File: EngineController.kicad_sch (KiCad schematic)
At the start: 35 parts, among them J1 RBUS, U1 ESP32-S3, Y1 R940000171

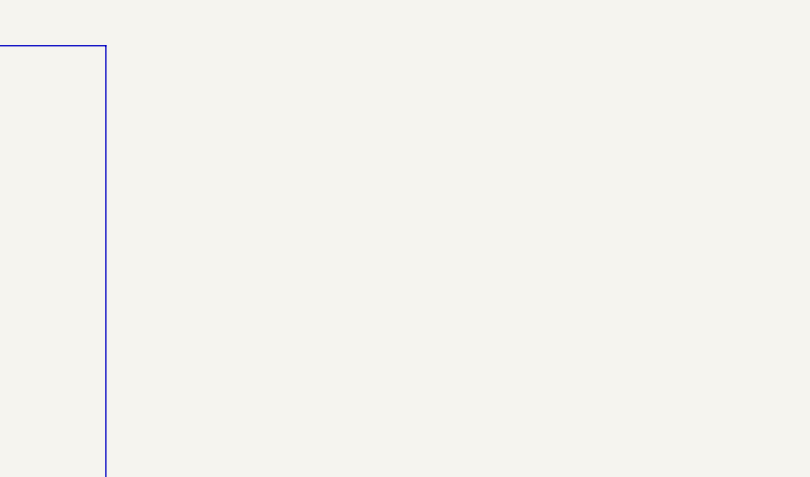
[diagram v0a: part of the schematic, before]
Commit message: Engine Controller Board: Added in Buck
Added in buck for chad and modified resistors to have output of 7.4V and 6V instead of 8.4V
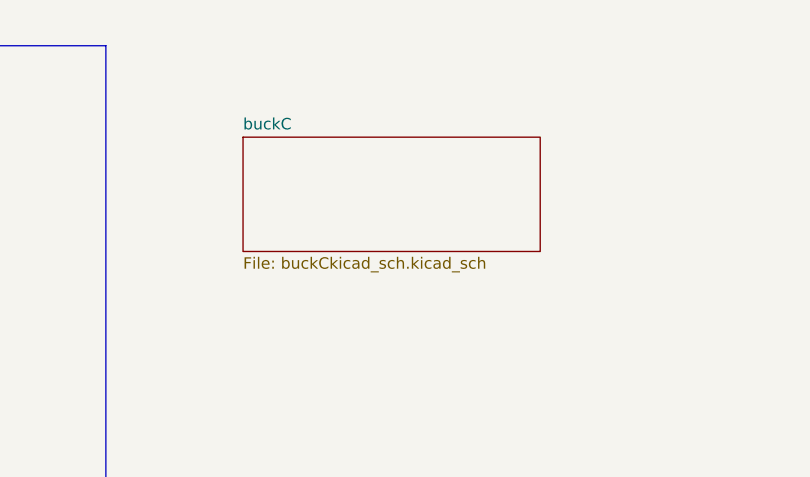
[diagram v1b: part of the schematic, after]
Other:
- added sheet buckC (buckCkicad_sch.kicad_sch)

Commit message: Xavier: Updated Engine Controller
Added in the actuators
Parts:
- added R25: 2.2k, Resistor_SMD:R_0402_1005Metric, symbol Device:R_Small
- added R5: 1.5k, Resistor_SMD:R_0402_1005Metric, symbol Device:R_Small
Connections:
- net GND: now also R25.1
- net BuckPGOOD: now reaches U1.37 (SPICLK_P/GPIO47)
- net BuckPGOOD: now also R25.2, R5.1
- net Servo1PWM: now reaches U1.41 (GPIO36)
- net Servo2PWM: now reaches U1.42 (GPIO37)
- net BUCK_EN: now reaches U1.43 (GPIO38)
- new net buckC/PGOOD: R5.2
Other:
- added sheet actuators (actuators.kicad_sch)
- sheet buckC ports: added BUCK_EN, PGOOD; removed none
- note added: "ServoV_LOG"
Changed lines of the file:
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@@
+    (stroke (width 0) (type default))
+  )
+  (wire (pts (xy 213.36 58.42) (xy 219.71 58.42))
     (stroke (width 0) (type default))
   )
@@
     (stroke (width 0) (type default))
   )
+  (wire (pts (xy 213.36 54.61) (xy 219.71 54.61))
+    (stroke (width 0) (type default))
+  )
   (wire (pts (xy 16.51 170.18) (xy 16.51 171.45))
     (stroke (width 0) (type default))
@@
     (stroke (width 0) (type default))
   )
+  (wire (pts (xy 213.36 62.23) (xy 219.71 62.23))
+    (stroke (width 0) (type default))
+  )
   (wire (pts (xy 44.45 135.89) (xy 46.99 135.89))
     (stroke (width 0) (type default))
@@
     (stroke (width 0) (type default))
   )
+  (wire (pts (xy 218.44 30.48) (xy 218.44 34.29))
+    (stroke (width 0) (type default))
+  )
   (wire (pts (xy 278.13 33.02) (xy 273.05 33.02))
     (stroke (width 0) (type default))
@@
     (stroke (width 0) (type default))
   )
+  (wire (pts (xy 215.9 21.59) (xy 226.06 21.59))
+    (stroke (width 0) (type default))
+  )
   (wire (pts (xy 107.95 187.96) (xy 115.57 187.96))
     (stroke (width 0) (type default))
@@
   )
   (wire (pts (xy 34.29 140.97) (xy 46.99 140.97))
+    (stroke (width 0) (type default))
+  )
+  (wire (pts (xy 215.9 25.4) (xy 218.44 25.4))
     (stroke (width 0) (type default))
   )
@@
     (effects (font (size 1.27 1.27)) (justify left bottom))
   )
+  (text "ServoV_LOG" (at 219.71 62.23 0)
+    (effects (font (size 1.27 1.27)) (justify left bottom))
+  )
   (text "CAN + is CAN High\nCAN - is CAN LOW\nNamed with a + and - as it\nis a KiCad requirement to\nroute differential tracks\n"
     (at 123.19 195.58 0)
@@
     (effects (font (size 1.27 1.27)) (justify right bottom))
   )
+  (text "ServoV_LOG" (at 135.89 100.33 0)
+    (effects (font (size 1.27 1.27)) (justify left bottom))
+  )
+  (label "Servo1PWM" (at 135.89 102.87 0) (fields_autoplaced)
+    (effects (font (size 1.27 1.27)) (justify left bottom))
+  )
   (label "CHIP_PU" (at 36.83 165.1 180) (fields_autoplaced)
     (effects (font (size 1.27 1.27)) (justify right bottom))
   )
+  (label "Servo1PWM" (at 219.71 58.42 0) (fields_autoplaced)
+    (effects (font (size 1.27 1.27)) (justify left bottom))
+  )
   (label "CAN+" (at 115.57 185.42 0) (fields_autoplaced)
     (effects (font (size 1.27 1.27)) (justify left bottom))
@@
     (effects (font (size 1.27 1.27)) (justify left bottom))
   )
+  (label "BuckPGOOD" (at 135.89 118.11 0) (fields_autoplaced)
+    (effects (font (size 1.27 1.27)) (justify left bottom))
+  )
   (label "RXD" (at 29.21 43.18 0) (fields_autoplaced)
+    (effects (font (size 1.27 1.27)) (justify left bottom))
+  )
+  (label "Servo2PWM" (at 219.71 54.61 0) (fields_autoplaced)
     (effects (font (size 1.27 1.27)) (justify left bottom))
   )
@@
     (effects (font (size 1.27 1.27)) (justify right bottom))
   )
+  (label "BUCK_EN" (at 226.06 21.59 180) (fields_autoplaced)
+    (effects (font (size 1.27 1.27)) (justify right bottom))
+  )
+  (label "BUCK_EN" (at 135.89 107.95 0) (fields_autoplaced)
+    (effects (font (size 1.27 1.27)) (justify left bottom))
+  )
   (label "RXD" (at 64.77 115.57 180) (fields_autoplaced)
     (effects (font (size 1.27 1.27)) (justify right bottom))
@@
     (effects (font (size 1.27 1.27)) (justify left bottom))
   )
+  (label "Servo2PWM" (at 135.89 105.41 0) (fields_autoplaced)
+    (effects (font (size 1.27 1.27)) (justify left bottom))
+  )
   (label "CAN_RX" (at 115.57 182.88 0) (fields_autoplaced)
     (effects (font (size 1.27 1.27)) (justify left bottom))
@@
   )
   (label "CAN-" (at 115.57 187.96 0) (fields_autoplaced)
+    (effects (font (size 1.27 1.27)) (justify left bottom))
+  )
+  (label "BuckPGOOD" (at 218.44 33.02 0) (fields_autoplaced)
     (effects (font (size 1.27 1.27)) (justify left bottom))
   )
@@
     )
   )
+  (symbol (lib_id "power:GND") (at 218.44 39.37 0) (unit 1)
+    (in_bom yes) (on_board yes) (dnp no)
+    (property "Reference" "#PWR028" (at 218.44 45.72 0)
+      (effects (font (size 1.27 1.27)) hide)
+    )
+    (property "Value" "GND" (at 218.567 43.7642 0)
+      (effects (font (size 1.27 1.27)))
+    )
+    (property "Footprint" "" (at 218.44 39.37 0)
+      (effects (font (size 1.27 1.27)) hide)
+    )
+    (property "Datasheet" "" (at 218.44 39.37 0)
+      (effects (font (size 1.27 1.27)) hide)
+    )
+    (pin "1")
+    (instances
+      (project "EngineController"
+        (path "/7db990e4-92e1-4f99-b4d2-435bbec1ba83"
+          (reference "#PWR028") (unit 1)
+        )
+      )
+    )
+  )
   (symbol (lib_id "power:GND") (at 167.64 132.08 0) (unit 1)
     (in_bom yes) (on_board yes) (dnp no)
@@
         (path "/7db990e4-92e1-4f99-b4d2-435bbec1ba83"
           (reference "#PWR011") (unit 1)
+        )
+      )
+    )
+  )
+  (symbol (lib_id "Device:R_Small") (at 218.44 27.94 180) (unit 1)
+    (in_bom yes) (on_board yes) (dnp no)
+    (property "Reference" "R5" (at 223.4184 27.94 90)
+      (effects (font (size 1.27 1.27)))
+    )
+    (property "Value" "1.5k" (at 221.107 27.94 90)
+      (effects (font (size 1.27 1.27)))
+    )
+    (property "Footprint" "Resistor_SMD:R_0402_1005Metric" (at 218.44 27.94 0)
+      (effects (font (size 1.27 1.27)) hide)
+    )
+    (property "Datasheet" "~" (at 218.44 27.94 0)
+      (effects (font (size 1.27 1.27)) hide)
+    )
+    (pin "1")
+    (pin "2")
+    (instances
+      (project "EngineController"
+        (path "/7db990e4-92e1-4f99-b4d2-435bbec1ba83"
+          (reference "R5") (unit 1)
         )
       )
@@
     )
   )
+  (symbol (lib_id "Device:R_Small") (at 218.44 36.83 180) (unit 1)
+    (in_bom yes) (on_board yes) (dnp no)
+    (property "Reference" "R25" (at 223.4184 36.83 90)
+      (effects (font (size 1.27 1.27)))
+    )
+    (property "Value" "2.2k" (at 221.107 36.83 90)
+      (effects (font (size 1.27 1.27)))
+    )
+    (property "Footprint" "Resistor_SMD:R_0402_1005Metric" (at 218.44 36.83 0)
+      (effects (font (size 1.27 1.27)) hide)
+    )
+    (property "Datasheet" "~" (at 218.44 36.83 0)
+      (effects (font (size 1.27 1.27)) hide)
+    )
+    (pin "1")
+    (pin "2")
+    (instances
+      (project "EngineController"
+        (path "/7db990e4-92e1-4f99-b4d2-435bbec1ba83"
+          (reference "R25") (unit 1)
+        )
+      )
+    )
+  )
   (symbol (lib_id "power:GND") (at 270.51 33.02 0) (unit 1)
     (in_bom yes) (on_board yes) (dnp no)
@@
     )
   )
-  (sheet (at 190.5 22.86) (size 33.02 12.7) (fields_autoplaced)
+  (sheet (at 182.88 49.53) (size 30.48 15.24) (fields_autoplaced)
     (stroke (width 0.1524) (type solid))
     (fill (color 0 0 0 0.0000))
-    (property "Sheetname" "buckC" (at 190.5 22.1484 0)
+    (property "Sheetname" "actuators" (at 182.88 48.8184 0)
       (effects (font (size 1.27 1.27)) (justify left bottom))
     )
-    (property "Sheetfile" "buckCkicad_sch.kicad_sch" (at 190.5 36.1446 0)
+    (property "Sheetfile" "actuators.kicad_sch" (at 182.88 65.3546 0)
       (effects (font (size 1.27 1.27)) (justify left top))
     )
-    (instances
+    (pin "SERVO2" bidirectional (at 213.36 54.61 0)
+      (effects (font (size 1.27 1.27)) (justify right))
+    )
+    (pin "SERVO1" bidirectional (at 213.36 58.42 0)
+      (effects (font (size 1.27 1.27)) (justify right))
+    )
+    (pin "SERVO_LOG" output (at 213.36 62.23 0)
+      (effects (font (size 1.27 1.27)) (justify right))
+    )
+    (instances
+      (project "EngineController"
+        (path "/7db990e4-92e1-4f99-b4d2-435bbec1ba83" (page "6"))
+      )
+    )
+  )
+  (sheet (at 182.88 17.78) (size 33.02 12.7) (fields_autoplaced)
+    (stroke (width 0.1524) (type solid))
+    (fill (color 0 0 0 0.0000))
+    (property "Sheetname" "buckC" (at 182.88 17.0684 0)
+      (effects (font (size 1.27 1.27)) (justify left bottom))
+    )
+    (property "Sheetfile" "buckCkicad_sch.kicad_sch" (at 182.88 31.0646 0)
+      (effects (font (size 1.27 1.27)) (justify left top))
+    )
+    (pin "PGOOD" output (at 215.9 25.4 0)
+      (effects (font (size 1.27 1.27)) (justify right))
+    )
+    (pin "BUCK_EN" input (at 215.9 21.59 0)
+      (effects (font (size 1.27 1.27)) (justify right))
+    )
+    (instances

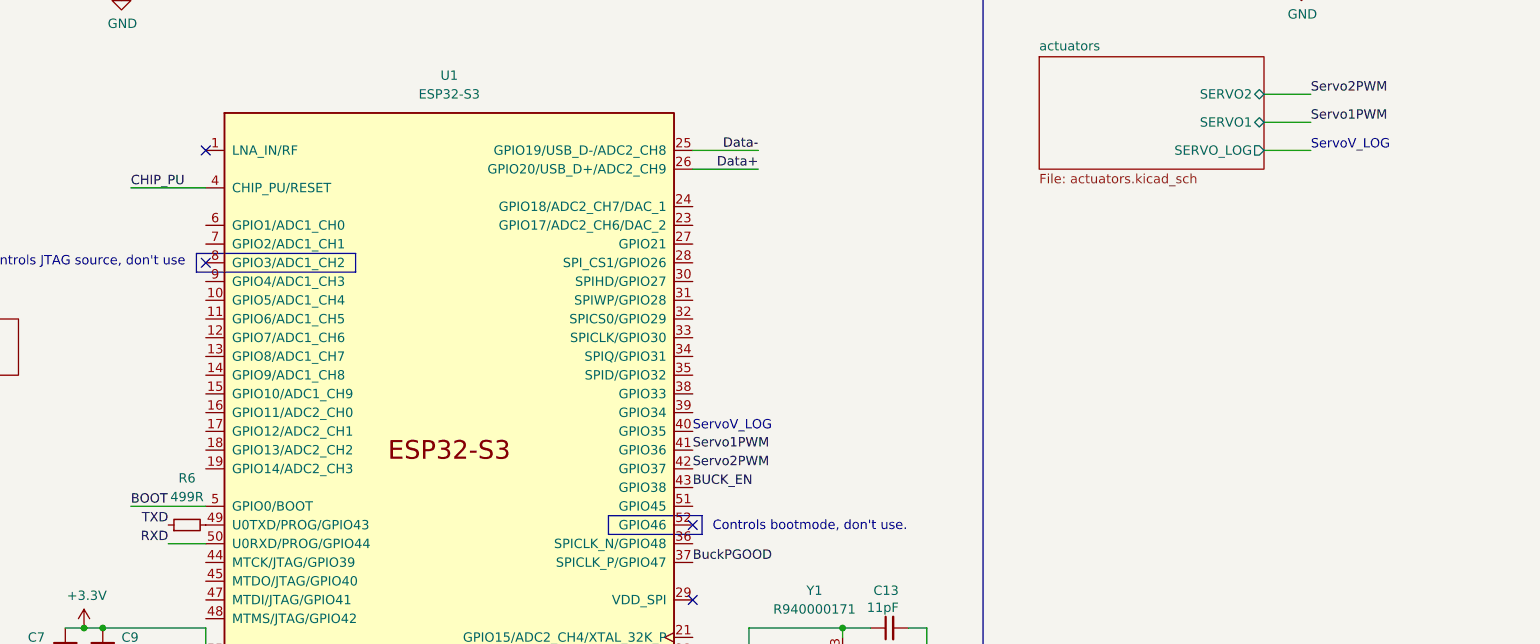
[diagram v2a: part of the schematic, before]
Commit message: Engine Controller: Added in ads and pressure sensor
Circuit for both 5v and 10v
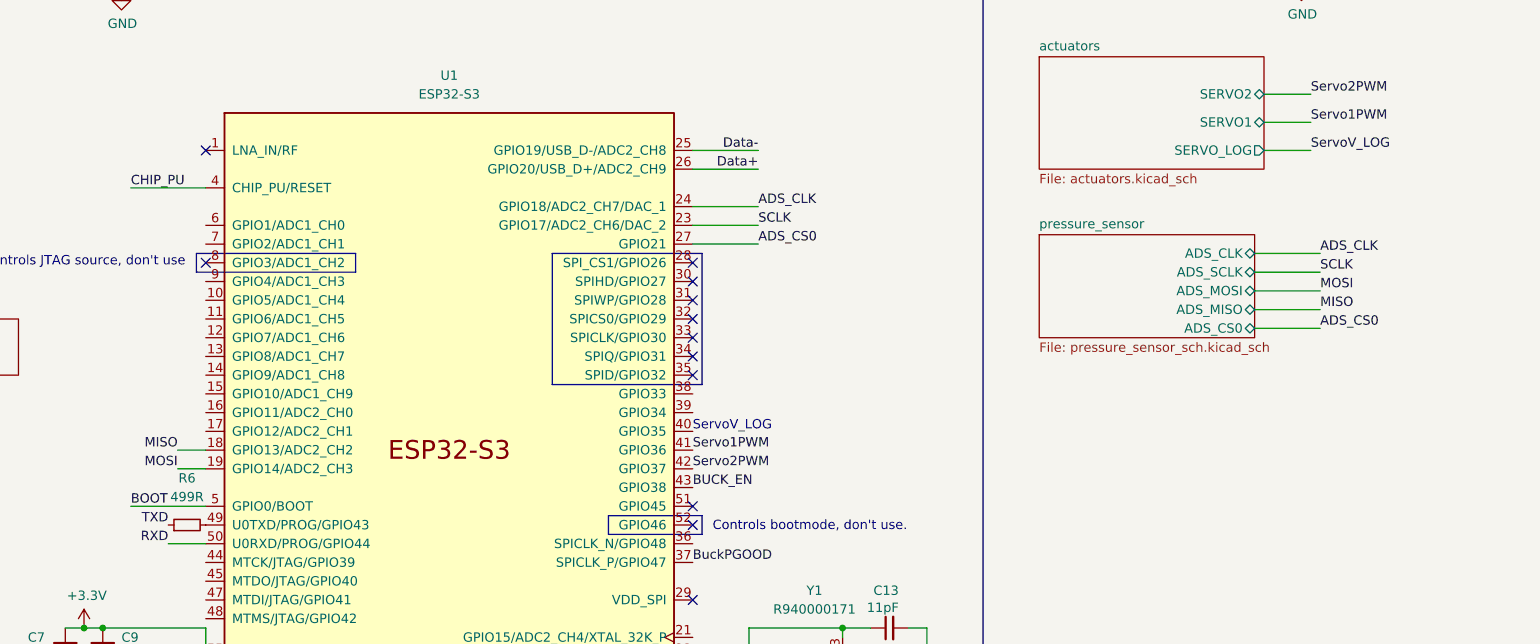
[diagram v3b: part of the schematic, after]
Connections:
- net MISO: now reaches U1.18 (GPIO13/ADC2_CH2)
- net MOSI: now reaches U1.19 (GPIO14/ADC2_CH3)
- net SCLK: now reaches U1.23 (GPIO17/ADC2_CH6/DAC_2)
- net ADS_CLK: now reaches U1.24 (GPIO18/ADC2_CH7/DAC_1)
- net ADS_CS0: now reaches U1.27 (GPIO21)
- no-connect marks 4 -> 12
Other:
- added sheet pressure_sensor (pressure_sensor_sch.kicad_sch)
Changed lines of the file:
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@@
   (junction (at 69.85 135.89) (diameter 0) (color 0 0 0 0)
   )
+  (no_connect (at 135.89 90.17))
+  (no_connect (at 135.89 82.55))
+  (no_connect (at 135.89 80.01))
   (no_connect (at 69.85 77.47))
+  (no_connect (at 135.89 85.09))
   (no_connect (at 69.85 62.23))
   (no_connect (at 135.89 113.03))
+  (no_connect (at 135.89 87.63))
+  (no_connect (at 135.89 92.71))
+  (no_connect (at 135.89 77.47))
   (no_connect (at 135.89 123.19))
+  (no_connect (at 135.89 110.49))
   (wire (pts (xy 30.48 191.77) (xy 30.48 190.5))
     (stroke (width 0) (type default))
@@
     (stroke (width 0) (type default))
   )
+  (wire (pts (xy 212.09 83.82) (xy 220.98 83.82))
+    (stroke (width 0) (type default))
+  )
+  (wire (pts (xy 212.09 81.28) (xy 220.98 81.28))
+    (stroke (width 0) (type default))
+  )
+  (wire (pts (xy 66.04 105.41) (xy 69.85 105.41))
+    (stroke (width 0) (type default))
+  )
   (wire (pts (xy 160.02 127) (xy 156.21 127))
     (stroke (width 0) (type default))
@@
     (stroke (width 0) (type default))
   )
+  (polyline (pts (xy 137.16 76.2) (xy 137.16 93.98))
+    (stroke (width 0) (type default))
+  )
   (wire (pts (xy 29.21 135.89) (xy 34.29 135.89))
     (stroke (width 0) (type default))
@@
     (stroke (width 0) (type default))
   )
+  (wire (pts (xy 135.89 72.39) (xy 144.78 72.39))
+    (stroke (width 0) (type default))
+  )
   (wire (pts (xy 57.15 147.32) (xy 59.69 147.32))
     (stroke (width 0) (type default))
@@
     (stroke (width 0) (type default))
   )
+  (polyline (pts (xy 137.16 93.98) (xy 116.84 93.98))
+    (stroke (width 0) (type default))
+  )
   (wire (pts (xy 156.21 127) (xy 156.21 128.27))
     (stroke (width 0) (type default))
@@
     (stroke (width 0) (type default))
   )
+  (wire (pts (xy 212.09 76.2) (xy 220.98 76.2))
+    (stroke (width 0) (type default))
+  )
   (wire (pts (xy 69.85 130.81) (xy 69.85 133.35))
     (stroke (width 0) (type default))
@@
     (stroke (width 0) (type default))
   )
+  (polyline (pts (xy 116.84 76.2) (xy 116.84 93.98))
+    (stroke (width 0) (type default))
+  )
   (wire (pts (xy 278.13 33.02) (xy 273.05 33.02))
     (stroke (width 0) (type default))
@@
     (stroke (width 0) (type default))
   )
+  (polyline (pts (xy 137.16 76.2) (xy 116.84 76.2))
+    (stroke (width 0) (type default))
+  )
+  (wire (pts (xy 212.09 78.74) (xy 220.98 78.74))
+    (stroke (width 0) (type default))
+  )
   (wire (pts (xy 167.64 127) (xy 167.64 132.08))
     (stroke (width 0) (type default))
@@
     (stroke (width 0) (type default))
   )
+  (wire (pts (xy 135.89 69.85) (xy 144.78 69.85))
+    (stroke (width 0) (type default))
+  )
   (wire (pts (xy 53.34 127) (xy 55.88 127))
     (stroke (width 0) (type default))
@@
     (stroke (width 0) (type default))
   )
+  (wire (pts (xy 66.04 102.87) (xy 69.85 102.87))
+    (stroke (width 0) (type default))
+  )
   (wire (pts (xy 69.85 142.24) (xy 69.85 140.97))
     (stroke (width 0) (type default))
@@
     (stroke (width 0) (type default))
   )
+  (wire (pts (xy 135.89 74.93) (xy 144.78 74.93))
+    (stroke (width 0) (type default))
+  )
   (wire (pts (xy 16.51 165.1) (xy 24.13 165.1))
     (stroke (width 0) (type default))
   )
   (polyline (pts (xy 175.26 198.12) (xy 12.7 198.12))
+    (stroke (width 0) (type default))
+  )
+  (wire (pts (xy 212.09 86.36) (xy 220.98 86.36))
     (stroke (width 0) (type default))
   )
@@
     (effects (font (size 1.27 1.27)) (justify left bottom))
   )
-  (text "ServoV_LOG" (at 219.71 62.23 0)
-    (effects (font (size 1.27 1.27)) (justify left bottom))
-  )
   (text "CAN + is CAN High\nCAN - is CAN LOW\nNamed with a + and - as it\nis a KiCad requirement to\nroute differential tracks\n"
     (at 123.19 195.58 0)
@@
     (effects (font (size 1.27 1.27)) (justify left bottom))
   )
+  (label "MOSI" (at 220.98 81.28 0) (fields_autoplaced)
+    (effects (font (size 1.27 1.27)) (justify left bottom))
+  )
   (label "Servo1PWM" (at 135.89 102.87 0) (fields_autoplaced)
     (effects (font (size 1.27 1.27)) (justify left bottom))
@@
     (effects (font (size 1.27 1.27)) (justify left bottom))
   )
+  (label "MISO" (at 220.98 83.82 0) (fields_autoplaced)
+    (effects (font (size 1.27 1.27)) (justify left bottom))
+  )
+  (label "SCLK" (at 220.98 78.74 0) (fields_autoplaced)
+    (effects (font (size 1.27 1.27)) (justify left bottom))
+  )
   (label "CAN+" (at 115.57 185.42 0) (fields_autoplaced)
     (effects (font (size 1.27 1.27)) (justify left bottom))
   )
+  (label "ADS_CS0" (at 220.98 86.36 0) (fields_autoplaced)
+    (effects (font (size 1.27 1.27)) (justify left bottom))
+  )
   (label "Data+" (at 99.06 160.02 0) (fields_autoplaced)
     (effects (font (size 1.27 1.27)) (justify left bottom))
@@
   )
   (label "RXD" (at 29.21 43.18 0) (fields_autoplaced)
+    (effects (font (size 1.27 1.27)) (justify left bottom))
+  )
+  (label "MOSI" (at 66.04 105.41 180) (fields_autoplaced)
+    (effects (font (size 1.27 1.27)) (justify right bottom))
+  )
+  (label "SCLK" (at 144.78 72.39 0) (fields_autoplaced)
     (effects (font (size 1.27 1.27)) (justify left bottom))
   )
@@
     (effects (font (size 1.27 1.27)) (justify right bottom))
   )
+  (label "ADS_CLK" (at 144.78 69.85 0) (fields_autoplaced)
+    (effects (font (size 1.27 1.27)) (justify left bottom))
+  )
+  (label "MISO" (at 66.04 102.87 180) (fields_autoplaced)
+    (effects (font (size 1.27 1.27)) (justify right bottom))
+  )
   (label "TXD" (at 29.21 38.1 0) (fields_autoplaced)
     (effects (font (size 1.27 1.27)) (justify left bottom))
@@
     (effects (font (size 1.27 1.27)) (justify right bottom))
   )
+  (label "ADS_CS0" (at 144.78 74.93 0) (fields_autoplaced)
+    (effects (font (size 1.27 1.27)) (justify left bottom))
+  )
+  (label "ADS_CLK" (at 220.98 76.2 0) (fields_autoplaced)
+    (effects (font (size 1.27 1.27)) (justify left bottom))
+  )
   (label "CHIP_PU" (at 59.69 67.31 0) (fields_autoplaced)
+    (effects (font (size 1.27 1.27)) (justify left bottom))
+  )
+  (label "ServoV_LOG" (at 219.71 62.23 0) (fields_autoplaced)
     (effects (font (size 1.27 1.27)) (justify left bottom))
   )
@@
       )
     )
+  )
+  (sheet (at 182.88 73.66) (size 29.21 13.97) (fields_autoplaced)
+    (stroke (width 0.1524) (type solid))
+    (fill (color 0 0 0 0.0000))
+    (property "Sheetname" "pressure_sensor" (at 182.88 72.9484 0)
+      (effects (font (size 1.27 1.27)) (justify left bottom))
+    )
+    (property "Sheetfile" "pressure_sensor_sch.kicad_sch" (at 182.88 88.2146 0)
+      (effects (font (size 1.27 1.27)) (justify left top))
+    )
+    (pin "ADS_CLK" bidirectional (at 212.09 76.2 0)
+      (effects (font (size 1.27 1.27)) (justify right))
+    )
+    (pin "ADS_SCLK" bidirectional (at 212.09 78.74 0)
+      (effects (font (size 1.27 1.27)) (justify right))
+    )
+    (pin "ADS_MOSI" bidirectional (at 212.09 81.28 0)
+      (effects (font (size 1.27 1.27)) (justify right))
+    )
+    (pin "ADS_MISO" bidirectional (at 212.09 83.82 0)
+      (effects (font (size 1.27 1.27)) (justify right))
+    )
+    (pin "ADS_CS0" bidirectional (at 212.09 86.36 0)
+      (effects (font (size 1.27 1.27)) (justify right))
+    )
+    (instances
+      (project "EngineController"
+        (path "/7db990e4-92e1-4f99-b4d2-435bbec1ba83" (page "7"))
+      )
+    )

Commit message: Completed schematics
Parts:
- renumbered C13 to C12, C14 to C13, R6 to R5, R7 to R6, R5 to R7, R25 to R8, TP9 to TP1, TP10 to TP2
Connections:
- net CAN_RX: now also U1.39 (GPIO34)
- net CAN_TX: now also U1.38 (GPIO33)
- net ServoV_LOG: now also U1.40 (GPIO35)
- no-connect marks 12 -> 30
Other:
- added sheet Boosts (boosts_sch.kicad_sch)
- note removed: "ServoV_LOG"
